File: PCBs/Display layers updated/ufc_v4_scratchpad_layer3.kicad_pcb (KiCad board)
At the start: 2 copper layers, 58 x 16.8 mm, 0 parts

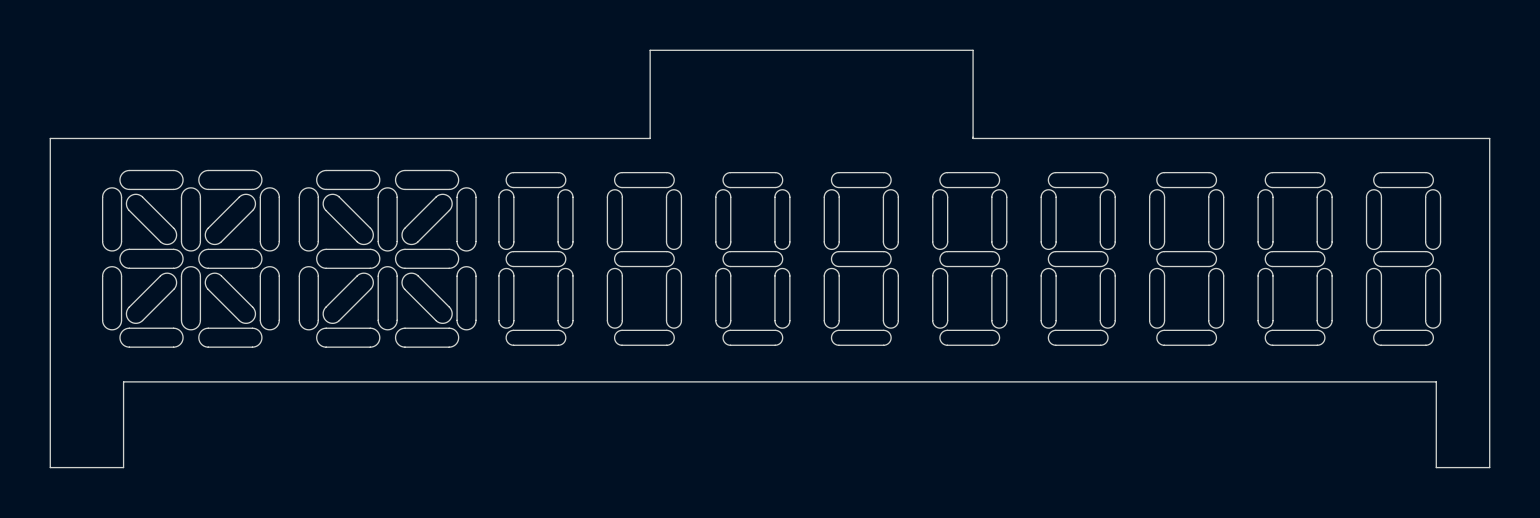
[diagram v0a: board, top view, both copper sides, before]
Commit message: Updated PCBs, cleaned up files
No commit for a while; a lot has happened in the mean time. JLC refused my order for the display layers, so I settled for just the dot layer. The gerbers for the rest are deleted, but the kicad files are still present.

I also received the main PCBs from JLC, and edited a couple small details.
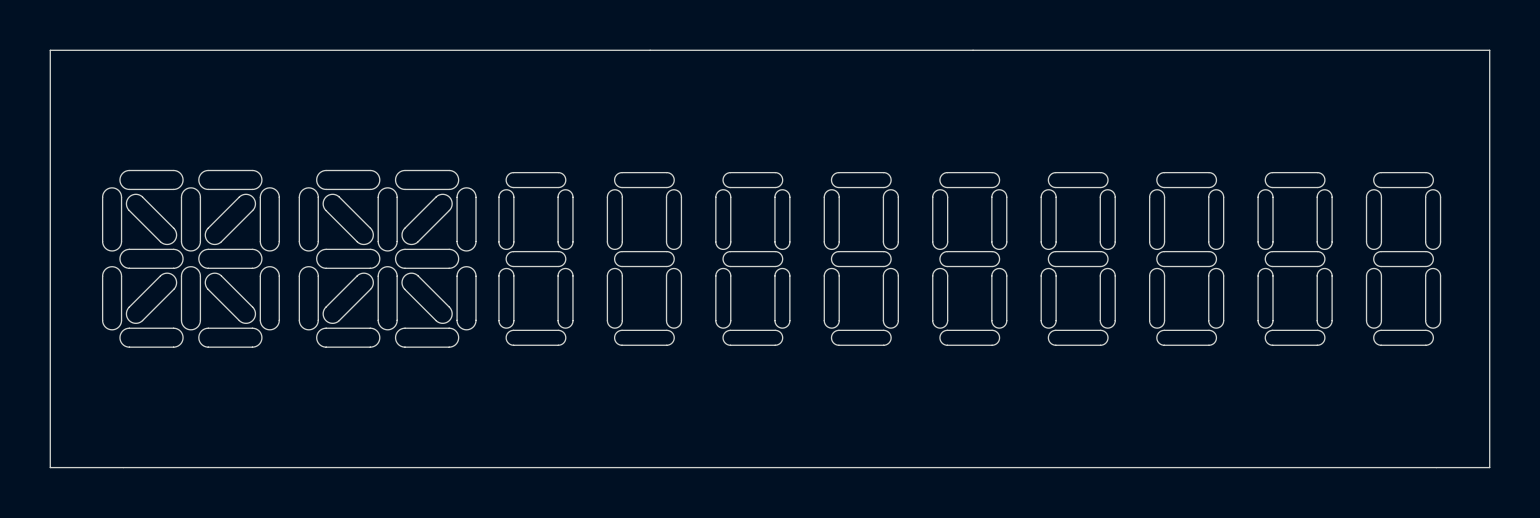
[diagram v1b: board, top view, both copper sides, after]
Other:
- outline, holes or cut-outs redrawn
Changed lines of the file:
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@@
   (general
     (thickness 1.6)
-    (drawings 396)
+    (drawings 391)
     (tracks 0)
     (zones 0)
@@
       (usegerberattributes false)
       (usegerberadvancedattributes false)
-      (creategerberjobfile false)
+      (creategerberjobfile true)
       (excludeedgelayer true)
       (linewidth 0.100000)
@@
       (drillshape 0)
       (scaleselection 1)
-      (outputdirectory "gerber"))
+      (outputdirectory "../Gerbers/Display layers/Scratchpad layer 3/"))
   )
   (net 0 "")
@@
   (gr_arc (start 119.928618 89.038382) (end 120.198026 89.30779) (angle -180) (layer Edge.Cuts) (width 0.05))
   (gr_line (start 115.225 96.484) (end 118.175 96.484) (layer Edge.Cuts) (width 0.05))
-  (gr_line (start 115.225 83.234) (end 115.225 96.484) (layer Edge.Cuts) (width 0.05))
+  (gr_line (start 115.225 79.684) (end 115.225 96.484) (layer Edge.Cuts) (width 0.05))
   (gr_line (start 139.375 79.684) (end 152.375 79.684) (layer Edge.Cuts) (width 0.05))
   (gr_line (start 173.175 96.484) (end 171.025 96.484) (layer Edge.Cuts) (width 0.05))
-  (gr_line (start 173.175 83.234) (end 173.175 96.484) (layer Edge.Cuts) (width 0.05))
-  (gr_line (start 171.025 93.034) (end 171.025 96.484) (layer Edge.Cuts) (width 0.05))
-  (gr_line (start 118.175 93.034) (end 171.025 93.034) (layer Edge.Cuts) (width 0.05))
-  (gr_line (start 118.175 96.484) (end 118.175 93.034) (layer Edge.Cuts) (width 0.05))
-  (gr_line (start 152.375 83.234) (end 173.175 83.234) (layer Edge.Cuts) (width 0.05))
-  (gr_line (start 152.375 83.184) (end 152.375 83.234) (layer Edge.Cuts) (width 0.05))
-  (gr_line (start 152.375 79.684) (end 152.375 83.184) (layer Edge.Cuts) (width 0.05))
-  (gr_line (start 139.375 83.234) (end 139.375 79.684) (layer Edge.Cuts) (width 0.05))
-  (gr_line (start 115.225 83.234) (end 139.375 83.234) (layer Edge.Cuts) (width 0.05))
+  (gr_line (start 173.175 79.684) (end 173.175 96.484) (layer Edge.Cuts) (width 0.05))
+  (gr_line (start 118.175 96.484) (end 171.025 96.484) (layer Edge.Cuts) (width 0.05))
+  (gr_line (start 152.375 79.684) (end 173.175 79.684) (layer Edge.Cuts) (width 0.05))
+  (gr_line (start 115.225 79.684) (end 139.375 79.684) (layer Edge.Cuts) (width 0.05))
   (gr_text "THIS SIDE DOWN" (at 116.375 88.084 270) (layer B.SilkS)
     (effects (font (size 0.6 0.6) (thickness 0.15)) (justify mirror))
